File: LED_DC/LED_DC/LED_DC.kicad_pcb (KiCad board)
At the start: 2 copper layers, 49 parts, among them J1 Conn_01x04, J2 Display Port GPIO, J3 Conn_01x05, Q1 FDV304P, Q2 FDV304P, Q3 FDV304P, Q4 FDV304P, Q5 FDV304P, Q6 FDV304P, Q7 FDV304P, Q8 FDV304P, SW1 SW_Push_45deg, SW2 SW_Push_45deg, SW3 SW_Push_45deg, SW4 SW_Push_45deg, U1 74HC238, U2 ULN2803A, U3 KCSA02-136, U4 KCSA02-136, U5 KCSA02-136, U6 KCSA02-136, U7 KCSA02-136, U8 KCSA02-136, U9 KCSA02-136

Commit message: updated PCB.
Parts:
- J1, J2, J3, Q1, Q2, Q3, Q4, Q5, Q6, Q7, Q8, R1, R10, R11, R2, R3, R4, R5, R6, R7, R8, R9, TP1, U1, U2: moved to B.Cu
- moved J1 82.9 mm to (173.4, 113.7)
- moved R1 64.3 mm to (189.9, 90.7)
- moved D8 56.7 mm to (212.7, 87.0)
- moved R3 55.5 mm to (193.7, 95.2)
- moved R2 46.8 mm to (193.7, 99.7)
- moved J3 41.6 mm to (168.9, 115.6)
- moved SW2 32.5 mm to (210.2, 121.3)
- moved R11 32.2 mm to (192.6, 113.5)
- moved U1 29.6 mm to (249.6, 108.0), turned to 180 degrees
- moved SW4 29.3 mm to (228.0, 109.2)
- moved R10 29.2 mm to (192.6, 115.0)
- moved R9 26.2 mm to (192.6, 116.5)
- moved H3 23.3 mm to (257.8, 135.9)
- moved R8 23.2 mm to (192.6, 118.0)
- moved H4 21.0 mm to (165.7, 135.3)
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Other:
- board outline added: 98.4 x 98.4 mm

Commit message: Updated the pcb.
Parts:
- moved J3 85.7 mm to (253.4, 101.0)
- moved J1 77.7 mm to (249.6, 98.4)
- moved R2 55.3 mm to (192.4, 44.5), turned to 180 degrees
- moved R3 51.1 mm to (188.0, 44.5), turned to 180 degrees
- moved R1 46.9 mm to (197.5, 44.5)
- moved TP1 36.1 mm to (177.8, 91.6), turned to 90 degrees
- moved R4 34.7 mm to (191.3, 89.3), turned to 90 degrees
- moved R5 33.3 mm to (189.8, 89.3), turned to 90 degrees
- moved U1 32.0 mm to (224.8, 87.6), turned to 270 degrees
- moved R6 31.9 mm to (188.3, 89.3), turned to 90 degrees
- moved R7 30.7 mm to (186.8, 89.3), turned to 90 degrees
- moved R8 29.5 mm to (185.3, 89.3), turned to 90 degrees
- moved R9 28.5 mm to (183.8, 89.3), turned to 90 degrees
- moved R10 27.6 mm to (182.3, 89.3), turned to 90 degrees
- moved R11 26.9 mm to (180.8, 89.3), turned to 90 degrees
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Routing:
- net GND: track 0.00 -> 352.0 mm, vias 0 -> 1
- net +5V: track 0.00 -> 301.5 mm
- net G: track 0.00 -> 204.7 mm
- net F: track 0.00 -> 177.0 mm
- net A: track 0.00 -> 167.9 mm, vias 0 -> 1
- net D1: track 0.00 -> 163.0 mm
- net B: track 0.00 -> 158.7 mm, vias 0 -> 1
- net D6: track 0.00 -> 157.0 mm
- net D3: track 0.00 -> 156.5 mm
- net D5: track 0.00 -> 153.2 mm
- net D0: track 0.00 -> 151.0 mm, vias 0 -> 1
- net E: track 0.00 -> 148.4 mm
- net D7: track 0.00 -> 148.2 mm
- net C: track 0.00 -> 145.2 mm
- net D: track 0.00 -> 135.7 mm
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
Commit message: Updated PCB.
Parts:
- removed DS1: HY1602E, Connector_PinHeader_2.54mm:PinHeader_1x16_P2.54mm_Vertical
- removed J2: Display Port GPIO, Connector_PinHeader_2.54mm:PinHeader_2x05_P2.54mm_Vertical
- removed J3: Conn_01x05, Connector_PinHeader_2.54mm:PinHeader_1x05_P2.54mm_Vertical
- removed R1, R2, R3: R_Small, Resistor_SMD:R_0603_1608Metric
- D1, D2, D3, D4, D5, D6, D7, D8: footprint LED_SMD:LED_0603_1608Metric_Pad1.05x0.95mm_HandSolder -> LED_THT:LED_D3.0mm
- H1, H2, H3, H4: footprint MountingHole:MountingHole_2.2mm_M2_DIN965_Pad -> MountingHole:MountingHole_3.2mm_M3_DIN965_Pad
- J1: value Conn_01x04 -> MCU interface; footprint Connector_PinHeader_2.54mm:PinHeader_1x04_P2.54mm_Vertical -> Connector_PinHeader_2.54mm:PinHeader_2x10_P2.54mm_Vertical; moved to F.Cu
- moved H3 129.3 mm to (158.2, 53.4)
- moved H4 99.7 mm to (228.2, 57.5)
- moved U1 96.4 mm to (128.8, 96.4)
- moved Q6 80.4 mm to (136.9, 103.9), turned to 0 degrees
- moved J1 72.8 mm to (187.2, 60.9), turned to 90 degrees
- moved Q2 69.4 mm to (267.0, 82.1), turned to 0 degrees
- moved U7 68.8 mm to (168.8, 113.7), turned to 0 degrees
- moved U8 67.6 mm to (183.8, 113.7), turned to 0 degrees
- moved U9 65.3 mm to (200.3, 113.7), turned to 0 degrees
- moved Q1 59.5 mm to (112.0, 77.1), turned to 0 degrees
- moved H2 56.0 mm to (236.2, 95.5)
- moved U2 55.4 mm to (135.0, 78.3), turned to 0 degrees
- moved H1 52.3 mm to (158.4, 95.6)
- moved R4 45.8 mm to (146.2, 81.3), turned to 0 degrees
- moved R5 44.6 mm to (146.2, 79.8), turned to 0 degrees
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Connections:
- J1 pad 1: KEY_ROW1 -> +5V
- J1 pad 2: KEY_ROW2 -> +5V
- J1 pad 3: KEY_COL1 -> D0
- J1 pad 4: KEY_COL2 -> D1
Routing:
- net GND: track 352.0 -> 0.00 mm, vias 1 -> 0
- net +5V: track 301.5 -> 0.00 mm
- net G: track 204.7 -> 0.00 mm
- net F: track 177.0 -> 0.00 mm
- net A: track 167.9 -> 0.00 mm, vias 1 -> 0
- net D1: track 163.0 -> 0.00 mm
- net B: track 158.7 -> 0.00 mm, vias 1 -> 0
- net D6: track 157.0 -> 0.00 mm
- net D3: track 156.5 -> 0.00 mm
- net D5: track 153.2 -> 0.00 mm
- net D0: track 151.0 -> 0.00 mm, vias 1 -> 0
- net E: track 148.4 -> 0.00 mm
- net D7: track 148.2 -> 0.00 mm
- net C: track 145.2 -> 0.00 mm
- net D: track 135.7 -> 0.00 mm
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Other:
- board size 98.4 x 98.4 mm -> 86 x 48 mm

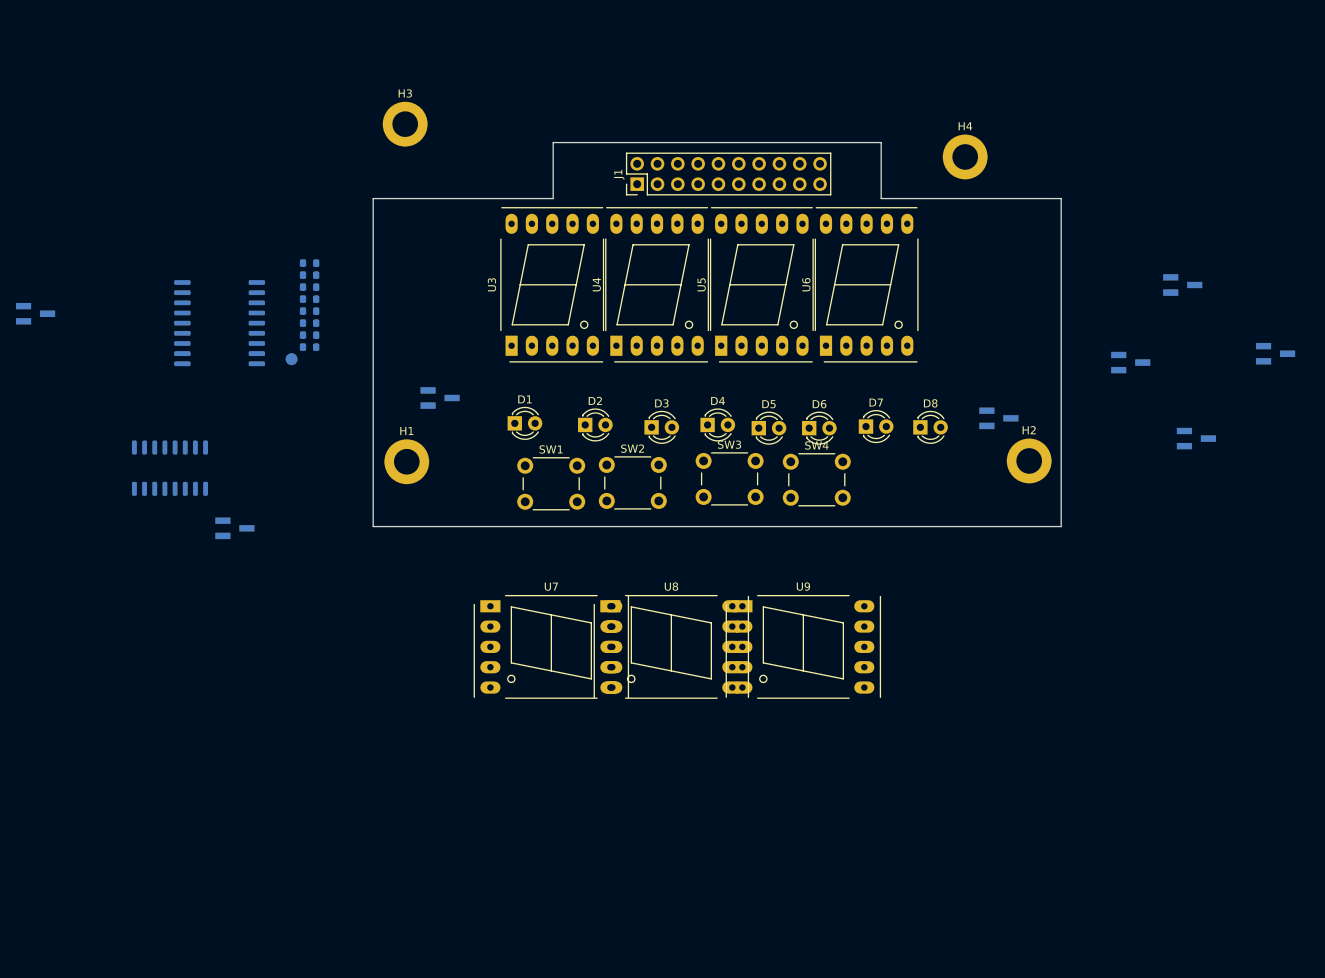
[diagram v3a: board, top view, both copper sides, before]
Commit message: Updated the LED DC PCB.
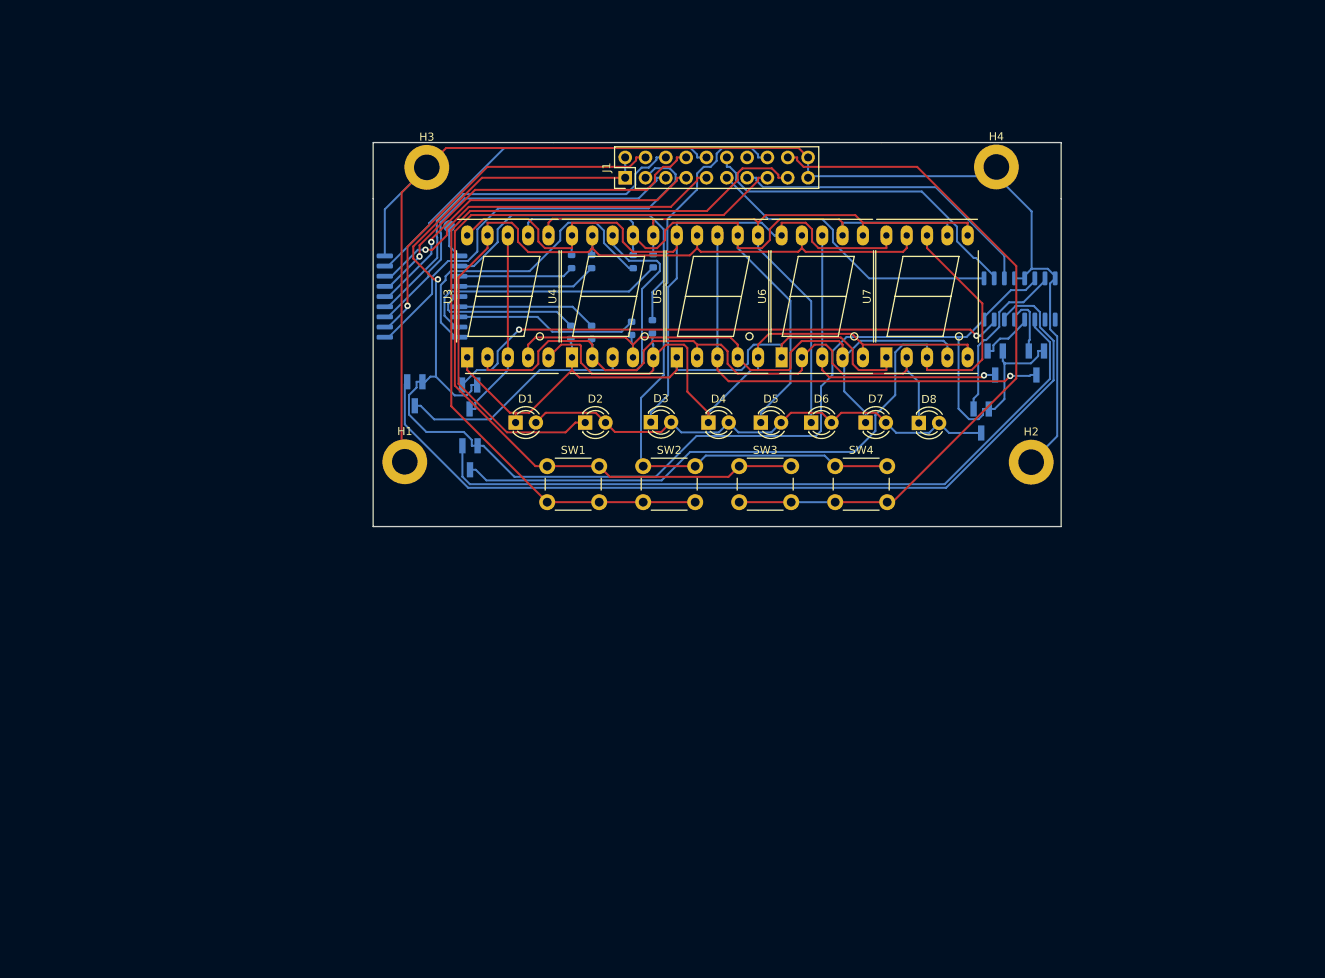
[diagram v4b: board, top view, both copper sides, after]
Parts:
- removed Q4, Q7: FDV304P, Package_TO_SOT_SMD:SOT-23_Handsoldering
- removed U8, U9: KCSA02-136, Display_7Segment:7SegmentLED_LTS6760_LTS6780
- moved U1 108.3 mm to (235.0, 75.2)
- moved Q6 97.3 mm to (231.9, 83.2), turned to 270 degrees
- moved Q3 91.7 mm to (166.3, 95.1), turned to 270 degrees
- moved U7 58.5 mm to (218.3, 82.5), turned to 90 degrees
- moved Q1 55.2 mm to (166.2, 87.5), turned to 270 degrees
- moved R5 43.9 mm to (189.2, 70.5), turned to 90 degrees
- moved R11 43.6 mm to (189.1, 78.7), turned to 270 degrees
- moved R4 41.8 mm to (186.7, 70.6), turned to 90 degrees
- moved R6 40.3 mm to (186.5, 78.9), turned to 270 degrees
- moved R9 35.4 mm to (181.5, 70.6), turned to 90 degrees
- moved R7 35.3 mm to (181.5, 79.4), turned to 270 degrees
- moved R8 32.9 mm to (178.9, 79.4), turned to 270 degrees
- moved R10 32.8 mm to (179.0, 70.6), turned to 90 degrees
- moved Q2 29.9 mm to (237.1, 83.2), turned to 270 degrees
- moved TP1 25.8 mm to (163.7, 66.2)
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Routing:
- net +5V: track 0.00 -> 191.1 mm, vias 0 -> 1
- net GND: track 0.00 -> 172.7 mm
- net D_C_2: track 0.00 -> 110.3 mm
- net KEY_ROW1: track 0.00 -> 108.6 mm
- net F: track 0.00 -> 105.9 mm
- net KEY_COL1: track 0.00 -> 104.0 mm
- net A: track 0.00 -> 99.2 mm
- net D_5: track 0.00 -> 98.0 mm
- net G: track 0.00 -> 97.9 mm
- net D_C_5: track 0.00 -> 91.3 mm
- net B: track 0.00 -> 90.5 mm
- net KEY_COL2: track 0.00 -> 89.5 mm
- net D: track 0.00 -> 83.3 mm
- net KEY_ROW2: track 0.00 -> 82.5 mm
- net DP: track 0.00 -> 80.2 mm
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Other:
- outline, holes or cut-outs redrawn

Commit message: Updated LED DC.
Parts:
- removed H3, H4: MountingHole_Pad, MountingHole:MountingHole_3.2mm_M3_DIN965_Pad
- removed TP1: TestPoint, TestPoint:TestPoint_Pad_D1.5mm
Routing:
- net KEY_ROW1: track 108.6 -> 70.5 mm, vias 0 -> 1
- net KEY_COL1: track 104.0 -> 70.2 mm, vias 0 -> 1
- net KEY_COL2: track 89.5 -> 103.4 mm
- net D_4: track 38.9 -> 52.4 mm, vias 1 -> 0
- net Net-(R4-Pad1): track 39.3 -> 26.0 mm, vias 0 -> 2
- net Net-(R5-Pad1): track 32.4 -> 43.7 mm
- net Net-(R11-Pad1): track 41.8 -> 30.9 mm
- net D_5: track 98.0 -> 88.4 mm
- net DP: track 80.2 -> 89.2 mm, vias 0 -> 1
- net +5V: track 191.1 -> 182.5 mm
- net D0: track 52.7 -> 44.6 mm, vias 0 -> 1
- net D_C_1: track 71.7 -> 78.6 mm
- net D_C_2: track 110.3 -> 104.3 mm
- net D_C_4: track 6.88 -> 12.6 mm
- net C: track 78.6 -> 74.0 mm
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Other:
- outline, holes or cut-outs redrawn
